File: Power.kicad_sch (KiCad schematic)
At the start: 58 parts, among them J1 Conn_01x01, J2 Conn_01x01, J3 Conn_01x01, Q1 2N7002, Q2 2N7002, Q3 2N7002, Q4 2N7002, Q5 2N7002, Q6 2N7002

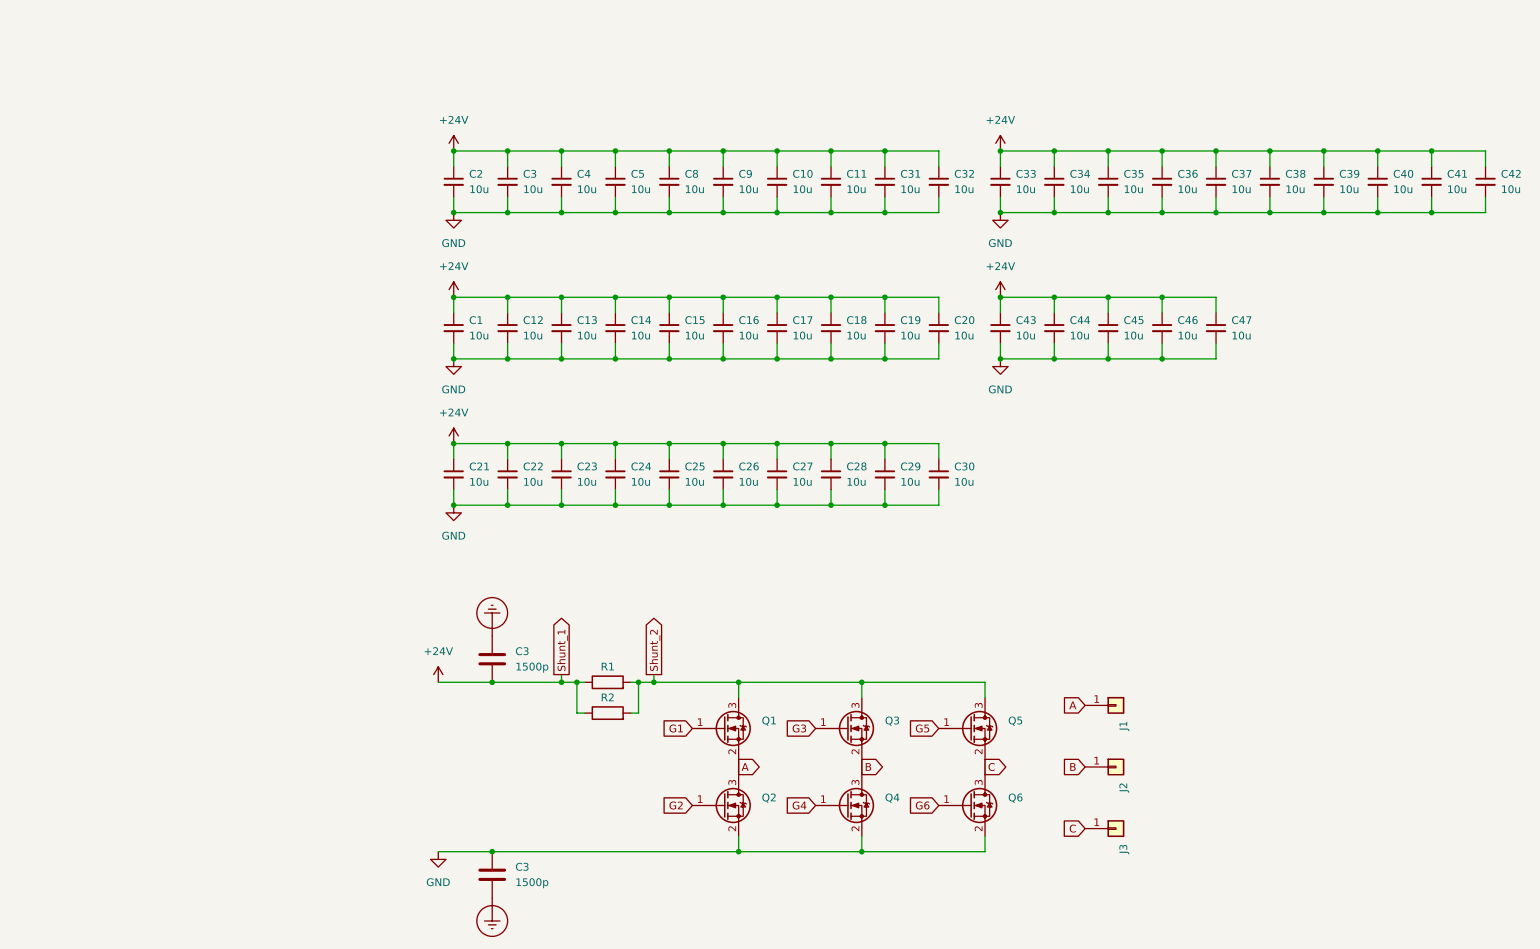
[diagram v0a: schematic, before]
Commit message: Поставил керамические Y конденсаторы
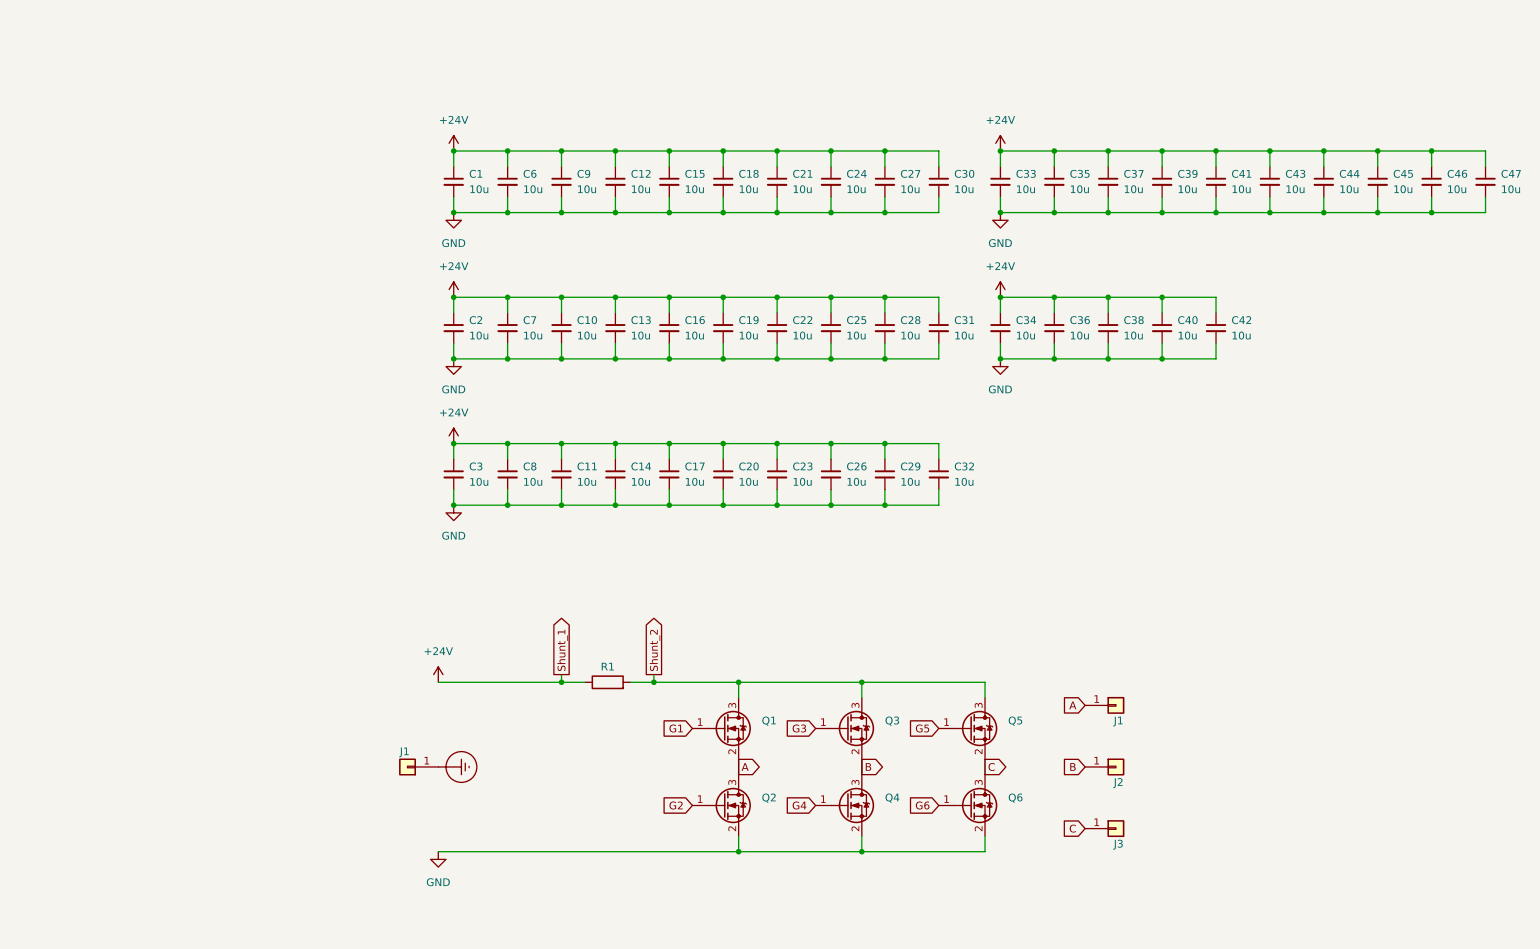
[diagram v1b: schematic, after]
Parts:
- removed C3 (x2): 1500p, Capacitor_THT:C_Rect_L10.0mm_W3.0mm_P7.50mm_FKS3_FKP3, symbol Device:C
- removed R2: R, Shunt_My:TLRS1050, symbol Device:R
- added J1: A, Connector_My:Power_Wire, symbol Connector_Generic:Conn_01x01
- J1: value Conn_01x01 -> A
- J2: value Conn_01x01 -> B
- J3: value Conn_01x01 -> C
- R1: value R -> PU2512FKGP60U5L; footprint Shunt_My:TLRS1050 -> Resistor_SMD:R_2512_6332Metric_Pad1.40x3.35mm_HandSolder
- renumbered C2 to C1, C13 to C10, C23 to C11, C5 to C12, C14 to C13, C24 to C14, C8 to C15, C15 to C16, C25 to C17, C9 to C18, C16 to C19, C1 to C2, C26 to C20, C10 to C21, C17 to C22, C27 to C23, C11 to C24, C18 to C25, C28 to C26, C31 to C27, C19 to C28, C21 to C3, C32 to C30, C20 to C31, C30 to C32, C43 to C34, C34 to C35, C44 to C36, C35 to C37, C45 to C38, C36 to C39, C46 to C40, C37 to C41, C47 to C42, C38 to C43, C39 to C44, C40 to C45, C41 to C46, C42 to C47, C3 to C6, C12 to C7, C22 to C8, C4 to C9
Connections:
- net Earth_Protective: now also J1.1 (Pin_1)

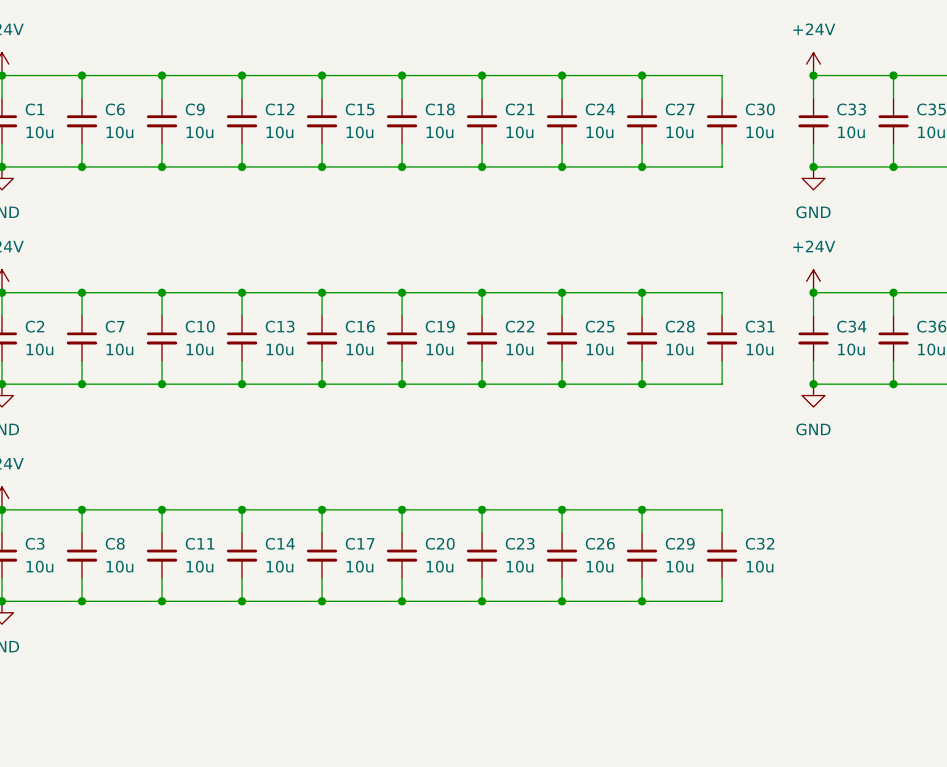
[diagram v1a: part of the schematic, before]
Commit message: Добавил крепежные отверстия
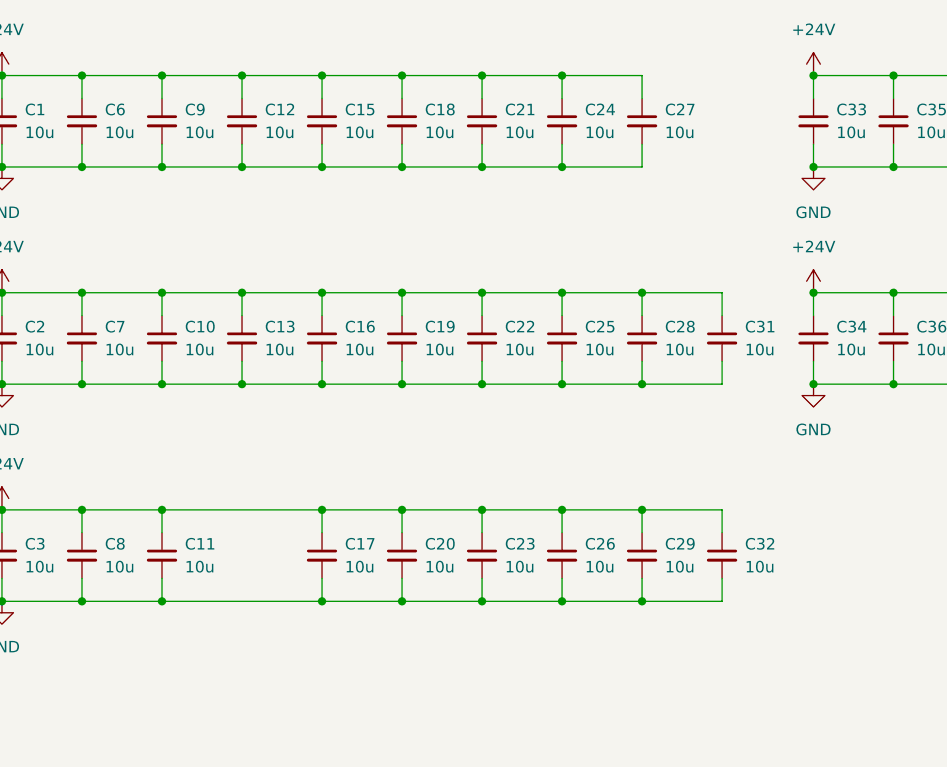
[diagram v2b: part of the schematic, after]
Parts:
- removed C14, C30: 10u, Capacitor_SMD:C_1210_3225Metric_Pad1.33x2.70mm_HandSolder, symbol Device:C_Small
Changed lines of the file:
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@@
   (junction (at 191.77 48.26) (diameter 0) (color 0 0 0 0)
   )
-  (junction (at 128.27 86.36) (diameter 0) (color 0 0 0 0)
-  )
   (junction (at 154.94 38.1) (diameter 0) (color 0 0 0 0)
   )
@@
   (junction (at 128.27 72.39) (diameter 0) (color 0 0 0 0)
   )
-  (junction (at 172.72 48.26) (diameter 0) (color 0 0 0 0)
-  )
   (junction (at 146.05 38.1) (diameter 0) (color 0 0 0 0)
   )
@@
   (junction (at 191.77 62.23) (diameter 0) (color 0 0 0 0)
   )
-  (junction (at 172.72 38.1) (diameter 0) (color 0 0 0 0)
-  )
   (junction (at 163.83 96.52) (diameter 0) (color 0 0 0 0)
   )
@@
   (junction (at 146.05 72.39) (diameter 0) (color 0 0 0 0)
   )
-  (junction (at 128.27 96.52) (diameter 0) (color 0 0 0 0)
-  )
   (junction (at 128.27 48.26) (diameter 0) (color 0 0 0 0)
   )
@@
     (stroke (width 0) (type default))
   )
-  (wire (pts (xy 128.27 86.36) (xy 137.16 86.36))
+  (wire (pts (xy 119.38 86.36) (xy 137.16 86.36))
     (stroke (width 0) (type default))
   )
@@
     (stroke (width 0) (type default))
   )
-  (wire (pts (xy 119.38 96.52) (xy 128.27 96.52))
-    (stroke (width 0) (type default))
-  )
   (wire (pts (xy 146.05 93.98) (xy 146.05 96.52))
     (stroke (width 0) (type default))
@@
     (stroke (width 0) (type default))
   )
-  (wire (pts (xy 172.72 48.26) (xy 181.61 48.26))
-    (stroke (width 0) (type default))
-  )
-  (wire (pts (xy 172.72 38.1) (xy 181.61 38.1))
-    (stroke (width 0) (type default))
-  )
   (wire (pts (xy 191.77 72.39) (xy 200.66 72.39))
     (stroke (width 0) (type default))
@@
     (stroke (width 0) (type default))
   )
-  (wire (pts (xy 181.61 45.72) (xy 181.61 48.26))
-    (stroke (width 0) (type default))
-  )
   (wire (pts (xy 209.55 38.1) (xy 218.44 38.1))
     (stroke (width 0) (type default))
@@
     (stroke (width 0) (type default))
   )
-  (wire (pts (xy 128.27 93.98) (xy 128.27 96.52))
-    (stroke (width 0) (type default))
-  )
   (wire (pts (xy 110.49 86.36) (xy 110.49 88.9))
     (stroke (width 0) (type default))
@@
     (stroke (width 0) (type default))
   )
-  (wire (pts (xy 181.61 40.64) (xy 181.61 38.1))
-    (stroke (width 0) (type default))
-  )
   (wire (pts (xy 110.49 72.39) (xy 119.38 72.39))
     (stroke (width 0) (type default))
@@
     (stroke (width 0) (type default))
   )
-  (wire (pts (xy 128.27 96.52) (xy 137.16 96.52))
+  (wire (pts (xy 119.38 96.52) (xy 137.16 96.52))
     (stroke (width 0) (type default))
   )
@@
     (stroke (width 0) (type default))
   )
-  (wire (pts (xy 119.38 86.36) (xy 128.27 86.36))
-    (stroke (width 0) (type default))
-  )
   (wire (pts (xy 99.06 125.73) (xy 119.38 125.73))
     (stroke (width 0) (type default))
@@
   )
   (wire (pts (xy 128.27 62.23) (xy 137.16 62.23))
-    (stroke (width 0) (type default))
-  )
-  (wire (pts (xy 128.27 88.9) (xy 128.27 86.36))
     (stroke (width 0) (type default))
   )
@@
         )
       )
-    )
-  )
-  (symbol (lib_id "Device:C_Small") (at 128.27 91.44 0) (unit 1)
-    (in_bom yes) (on_board yes) (dnp no) (fields_autoplaced)
-    (property "Reference" "C14" (at 130.81 90.1763 0)
-      (effects (font (size 1.27 1.27)) (justify left))
-    )
-    (property "Value" "10u" (at 130.81 92.7163 0)
-      (effects (font (size 1.27 1.27)) (justify left))
-    )
-    (property "Footprint" "Capacitor_SMD:C_1210_3225Metric_Pad1.33x2.70mm_HandSolder" (at 128.27 91.44 0)
-      (effects (font (size 1.27 1.27)) hide)
-    )
-    (property "Datasheet" "~" (at 128.27 91.44 0)
-      (effects (font (size 1.27 1.27)) hide)
-    )
-    (pin "1")
-    (pin "2")
-    (instances
-      (project "Силовая плата"
-        (path "/96c6fc92-8ec6-44f7-b0dc-9ad8f1acea09/c8b8118a-2e72-42b0-9c26-f9b5e594da69"
-          (reference "C14") (unit 1)
-        )
-      )
-    )
-  )
-  (symbol (lib_id "Device:C_Small") (at 181.61 43.18 0) (unit 1)
-    (in_bom yes) (on_board yes) (dnp no) (fields_autoplaced)
-    (property "Reference" "C30" (at 184.15 41.9163 0)
-      (effects (font (size 1.27 1.27)) (justify left))
-    )
-    (property "Value" "10u" (at 184.15 44.4563 0)
-      (effects (font (size 1.27 1.27)) (justify left))
-    )
-    (property "Footprint" "Capacitor_SMD:C_1210_3225Metric_Pad1.33x2.70mm_HandSolder" (at 181.61 43.18 0)
-      (effects (font (size 1.27 1.27)) hide)
-    )
-    (property "Datasheet" "~" (at 181.61 43.18 0)
-      (effects (font (size 1.27 1.27)) hide)
-    )
-    (pin "1")
-    (pin "2")
-    (instances
-      (project "Силовая плата"
-        (path "/96c6fc92-8ec6-44f7-b0dc-9ad8f1acea09/c8b8118a-2e72-42b0-9c26-f9b5e594da69"
-          (reference "C30") (unit 1)
-        )
-      )

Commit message: Добавил документы
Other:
- moved on the sheet: C1, C10, C11, C12, C13, C15, C16, C17, C18, C19, C2, C20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
